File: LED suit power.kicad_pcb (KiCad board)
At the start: 2 copper layers, 100 x 100 mm, 85 parts, among them J1 XT-60, J12 Conn_01x04_Male, J13 Conn_01x04_Male, J14 Conn_01x04_Male, J15 Conn_01x04_Male, J16 Conn_01x04_Male, J2 XT-60, J3 XT-60, J4 Conn_01x04_Male, J5 XT-60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

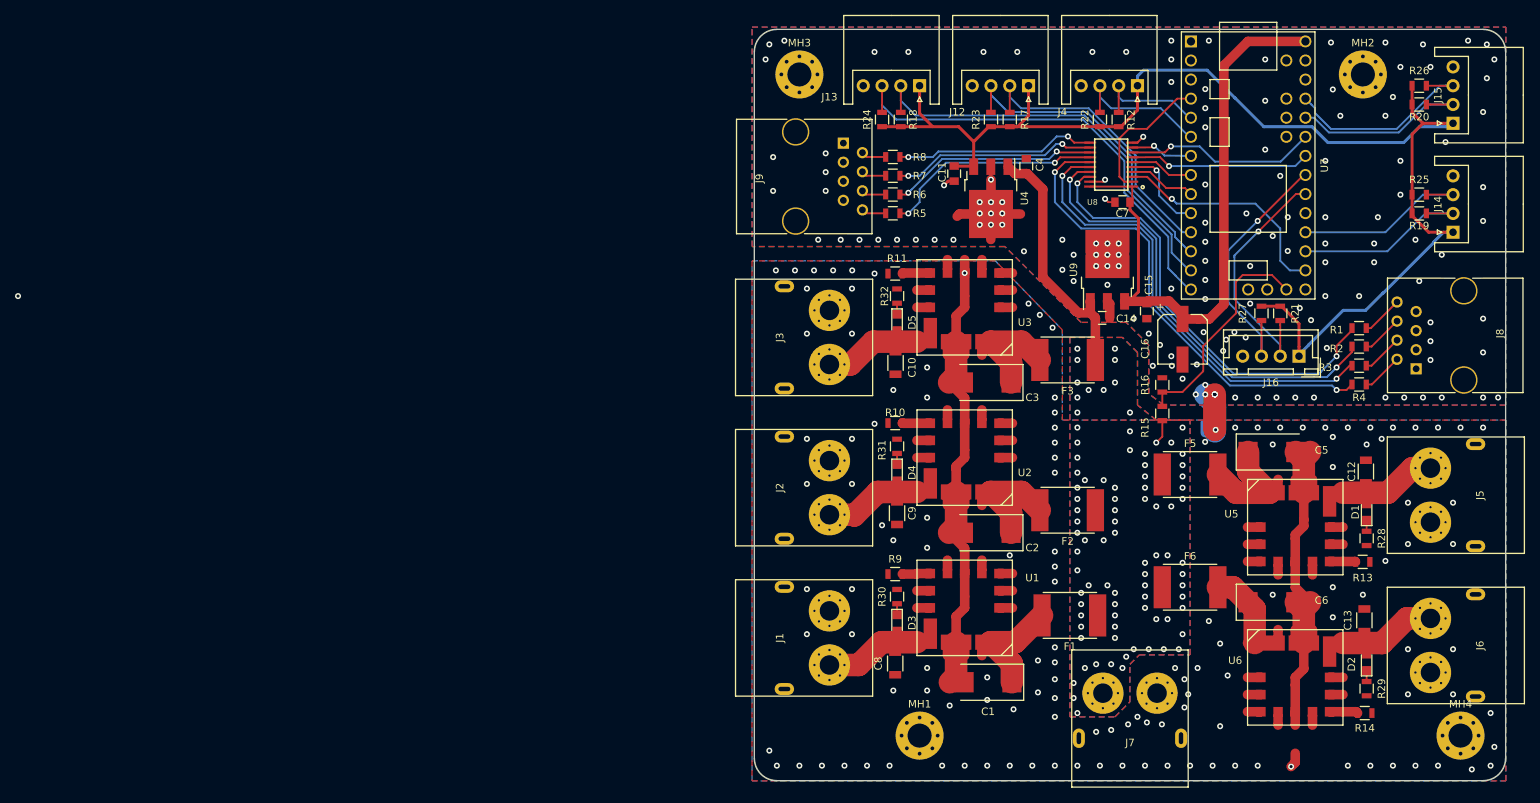
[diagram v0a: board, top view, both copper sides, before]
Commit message: reassigned pins for apa102 conversion
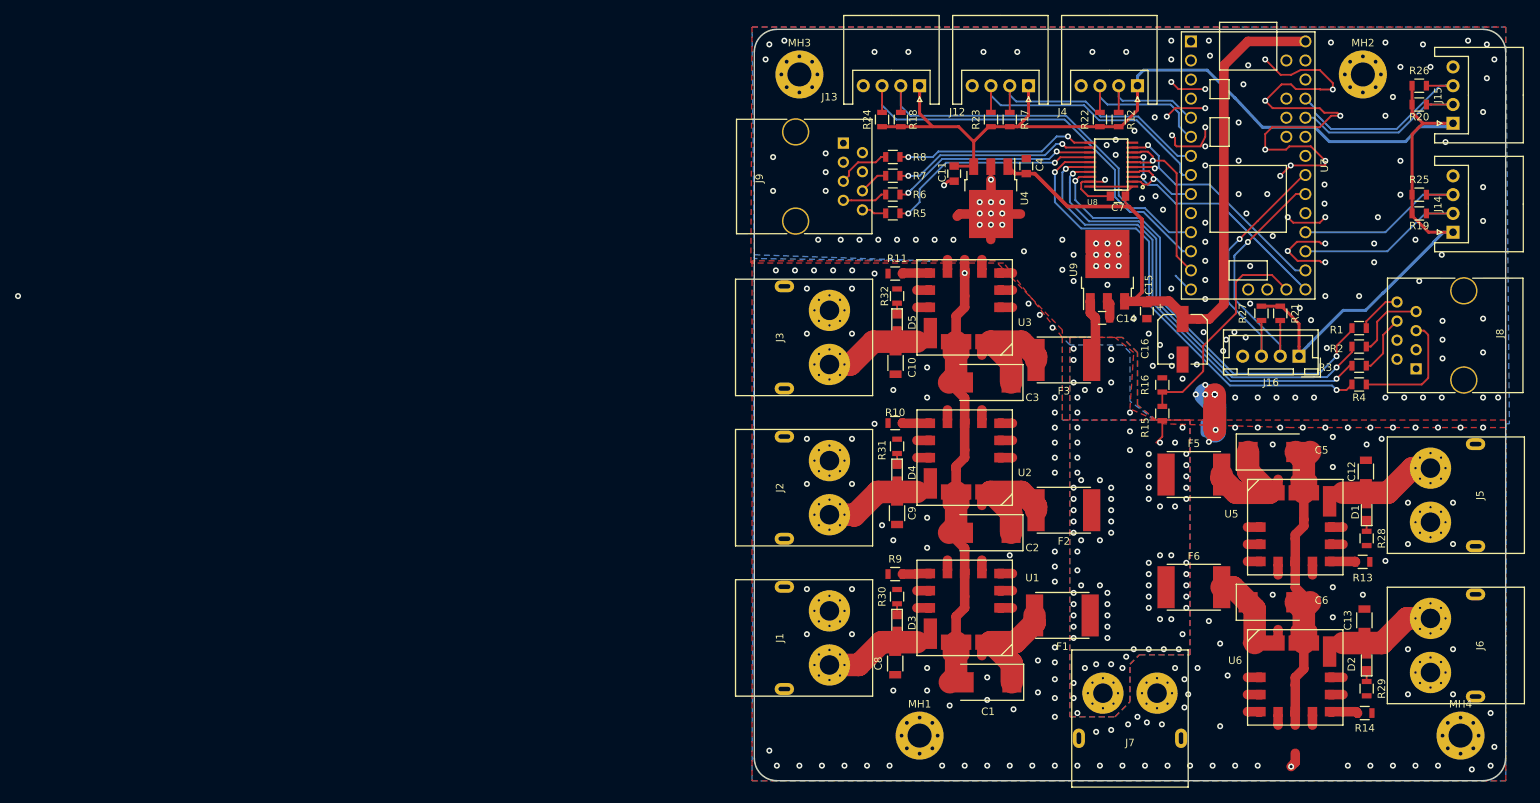
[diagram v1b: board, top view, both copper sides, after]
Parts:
- moved F1 1.00 mm to (141.0, 178.0)
- moved C7 1.00 mm to (148.4, 122.2)
- moved F2 0.50 mm to (141.2, 164.0)
- moved F3 0.50 mm to (141.2, 144.0)
- moved F5 0.50 mm to (158.5, 159.2)
- moved F6 0.50 mm to (158.5, 174.2)
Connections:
- C4 pad 1: VIN -> +5V
- J12 pad 2: PIN9 -> PIN5
- J12 pad 3: PIN10 -> PIN6
- J13 pad 2: PIN11 -> PIN9
- J13 pad 3: PIN12 -> PIN10
- J8 pad 1: GND -> Net-(J8-Pad1)
- J8 pad 3: GND -> Net-(J8-Pad3)
- J8 pad 5: GND -> Net-(J8-Pad5)
- J8 pad 7: GND -> Net-(J8-Pad7)
- J9 pad 1: GND -> Net-(J9-Pad1)
- J9 pad 3: GND -> Net-(J9-Pad3)
- J9 pad 5: GND -> Net-(J9-Pad5)
- J9 pad 7: GND -> Net-(J9-Pad7)
- R17 pad 1: PIN9 -> PIN5
- R18 pad 1: PIN11 -> PIN9
- R2 pad 1: Net-(J8-Pad6) -> Net-(J8-Pad7)
- R23 pad 1: PIN10 -> PIN6
- R24 pad 1: PIN12 -> PIN10
- R3 pad 1: Net-(J8-Pad4) -> Net-(J8-Pad6)
- R4 pad 1: Net-(J8-Pad2) -> Net-(J8-Pad5)
- R6 pad 1: Net-(J9-Pad6) -> Net-(J9-Pad7)
- R7 pad 1: Net-(J9-Pad4) -> Net-(J9-Pad6)
- R8 pad 1: Net-(J9-Pad2) -> Net-(J9-Pad5)
- U4 pad 1: VIN -> +5V
- U8 pad 2: PIN2 -> PIN7
- U8 pad 3: PIN14 -> PIN13
- U8 pad 5: PIN8 -> PIN14
- U8 pad 6: PIN6 -> PIN11
- U8 pad 7: PIN20 -> PIN13
- U8 pad 8: PIN21 -> PIN11
- U8 pad 9: PIN5 -> PIN14
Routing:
- net GND: track 137.5 -> 237.3 mm, vias 277 -> 296
- net PIN12: track 62.2 -> 2.59 mm
- net PIN13: track 0.00 -> 33.7 mm, vias 0 -> 2
- net PIN11: track 57.2 -> 24.1 mm, vias 0 -> 1
- net PIN6: track 8.31 -> 36.5 mm
- net VIN: track 37.2 -> 11.4 mm
- net PIN21: track 25.6 -> 0.00 mm, vias 1 -> 0
- net PIN20: track 24.1 -> 0.00 mm, vias 1 -> 0
- net PIN5: track 8.31 -> 32.3 mm, vias 1 -> 0
- net +5V: track 80.5 -> 100.6 mm
- net PIN2: track 18.6 -> 0.00 mm
- net Net-(J8-Pad5): track 0.00 -> 16.2 mm
- net PIN9: track 39.0 -> 53.9 mm
- net PIN10: track 42.7 -> 57.4 mm
- net PIN8: track 11.9 -> 0.00 mm, vias 1 -> 0
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
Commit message: i2c expander
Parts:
- added C17: 10uF, Capacitor_SMD:C_0805_2012Metric, F.Cu at (152.9, 115.7)
- added D6: D_Schottky, Diodes_SMD:D_PowerDI-123, F.Cu at (157.4, 138.0)
- added J10: Conn_01x03_Male, Connectors_JST:JST_XH_B03B-XH-A_03x2.50mm_Straight, F.Cu at (179.0, 119.8)
- added R33: 10k, Resistor_SMD:R_0805_2012Metric, F.Cu at (147.3, 114.5)
- added R34: 10k, Resistor_SMD:R_0805_2012Metric, F.Cu at (152.9, 118.8)
- added R35: 10k, Resistor_SMD:R_0805_2012Metric, F.Cu at (141.7, 116.3)
- added R36: 10k, Resistor_SMD:R_0805_2012Metric, F.Cu at (141.7, 114.4)
- added U10: TCA9548APWR, Package_SO:TSSOP-24_4.4x7.8mm_P0.65mm, F.Cu at (147.3, 119.7)
- moved C7 33.2 mm to (174.8, 142.4), turned to 90 degrees
- moved U8 32.7 mm to (170.1, 141.6), turned to 270 degrees
- moved R27 20.4 mm to (185.2, 127.8), turned to 0 degrees
- moved C16 18.7 mm to (144.3, 127.5), turned to 180 degrees
- moved R21 17.0 mm to (185.2, 130.2), turned to 0 degrees
- moved J16 11.9 mm to (179.0, 133.5), turned to 90 degrees
- moved C11 9.81 mm to (136.4, 118.8)
- moved C4 6.70 mm to (134.1, 124.5), turned to 180 degrees
- moved C14 5.27 mm to (151.6, 137.9), turned to 270 degrees
- moved C15 4.16 mm to (151.4, 133.4)
- moved U9 3.54 mm to (144.7, 134.7), turned to 180 degrees
- moved U4 2.86 mm to (129.9, 120.1), turned to 180 degrees
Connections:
- J12 pad 2: PIN5 -> Net-(J12-Pad2)
- J12 pad 3: PIN6 -> Net-(J12-Pad3)
- J13 pad 2: PIN9 -> Net-(J13-Pad2)
- J13 pad 3: PIN10 -> Net-(J13-Pad3)
- J14 pad 2: PIN15 -> Net-(J14-Pad2)
- J14 pad 3: PIN16 -> Net-(J14-Pad3)
- J15 pad 2: PIN22 -> Net-(J15-Pad2)
- J15 pad 3: PIN23 -> Net-(J15-Pad3)
- J4 pad 2: PIN3 -> Net-(J4-Pad2)
- J4 pad 3: PIN4 -> Net-(J4-Pad3)
- J8 pad 1: Net-(J8-Pad1) -> GND
- J8 pad 3: Net-(J8-Pad3) -> GND
- J8 pad 5: Net-(J8-Pad5) -> GND
- J8 pad 7: Net-(J8-Pad7) -> GND
- J9 pad 1: Net-(J9-Pad1) -> GND
- J9 pad 3: Net-(J9-Pad3) -> GND
- J9 pad 5: Net-(J9-Pad5) -> GND
- J9 pad 7: Net-(J9-Pad7) -> GND
- R12 pad 1: PIN3 -> Net-(J4-Pad2)
- R17 pad 1: PIN5 -> Net-(J12-Pad2)
- R18 pad 1: PIN9 -> Net-(J13-Pad2)
- R19 pad 1: PIN15 -> Net-(J14-Pad2)
- R2 pad 1: Net-(J8-Pad7) -> Net-(J8-Pad6)
- R20 pad 1: PIN22 -> Net-(J15-Pad2)
- R22 pad 1: PIN4 -> Net-(J4-Pad3)
- R23 pad 1: PIN6 -> Net-(J12-Pad3)
- R24 pad 1: PIN10 -> Net-(J13-Pad3)
- R25 pad 1: PIN16 -> Net-(J14-Pad3)
- R26 pad 1: PIN23 -> Net-(J15-Pad3)
- R3 pad 1: Net-(J8-Pad6) -> Net-(J8-Pad4)
- R4 pad 1: Net-(J8-Pad5) -> Net-(J8-Pad2)
- R6 pad 1: Net-(J9-Pad7) -> Net-(J9-Pad6)
- R7 pad 1: Net-(J9-Pad6) -> Net-(J9-Pad4)
- R8 pad 1: Net-(J9-Pad5) -> Net-(J9-Pad2)
- U7 pad 33: +5V -> Net-(D6-Pad1)
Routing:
- net Net-(J14-Pad2): track 0.00 -> 60.6 mm, vias 0 -> 1
- net Net-(J15-Pad2): track 0.00 -> 57.9 mm, vias 0 -> 2
- net PIN10: track 57.4 -> 0.00 mm
- net Net-(J14-Pad3): track 0.00 -> 54.8 mm, vias 0 -> 1
- net GND: track 237.3 -> 182.7 mm, vias 296 -> 292
- net Net-(J15-Pad3): track 0.00 -> 54.6 mm, vias 0 -> 2
- net PIN9: track 53.9 -> 0.00 mm
- net Net-(R4-Pad2): track 64.4 -> 11.9 mm, vias 2 -> 0
- net Net-(R3-Pad2): track 62.1 -> 11.7 mm, vias 2 -> 0
- net Net-(R2-Pad2): track 61.0 -> 11.6 mm, vias 2 -> 0
- net Net-(D6-Pad1): track 0.00 -> 48.6 mm
- net Net-(R1-Pad2): track 59.5 -> 12.7 mm, vias 2 -> 0
- net Net-(R8-Pad2): track 26.8 -> 66.6 mm
- net Net-(R7-Pad2): track 27.3 -> 66.9 mm
- net +5V: track 100.6 -> 62.2 mm
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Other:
- board text added: "(C) 2018 Chris Miller"
